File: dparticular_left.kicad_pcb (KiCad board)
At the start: 2 copper layers, 48 parts, among them J2 USB from outside, J3 To Right Hand, J4 Jumper to Teensy USB, SW1:6 Key_Scrl, SW1:7 Key_Paus, SW2:1 Key_ESC, SW2:2 Key_F1, SW2:3 Key_F2, SW2:4 Key_F3, SW2:5 Key_F4, SW2:6 Key_F5, SW2:7 Key_F6, SW3:1 Key_Home, SW3:2 Key_End, SW3:3 Key_Tilde, SW3:4 Key_1, SW3:5 Key_2, SW3:6 Key_3, SW3:7 Key_4, SW3:8 Key_5, SW4:2 Key_PgUp, SW4:3 Key_Tab, SW4:4 Key_Q, SW4:5 Key_W, SW4:6 Key_E, SW4:7 Key_R, SW4:8 Key_T, SW5:2 Key_PgDn, SW5:3 Key_Caps, SW5:4 Key_A, SW5:5 Key_S, SW5:6 Key_D, SW5:7 Key_F, SW5:8 Key_G, SW6:3 Key_LShft, SW6:4 Key_Z, SW6:5 Key_X, SW6:6 Key_C, SW6:7 Key_V, SW6:8 Key_B, SW7:3 Key_LCtrl, SW7:4 Key_Fn, SW7:5 Key_LWin, SW7:6 Key_LAlt, SW7:8 Key_LSpc, U2 TEENSY2.0_ONLY_EDGES

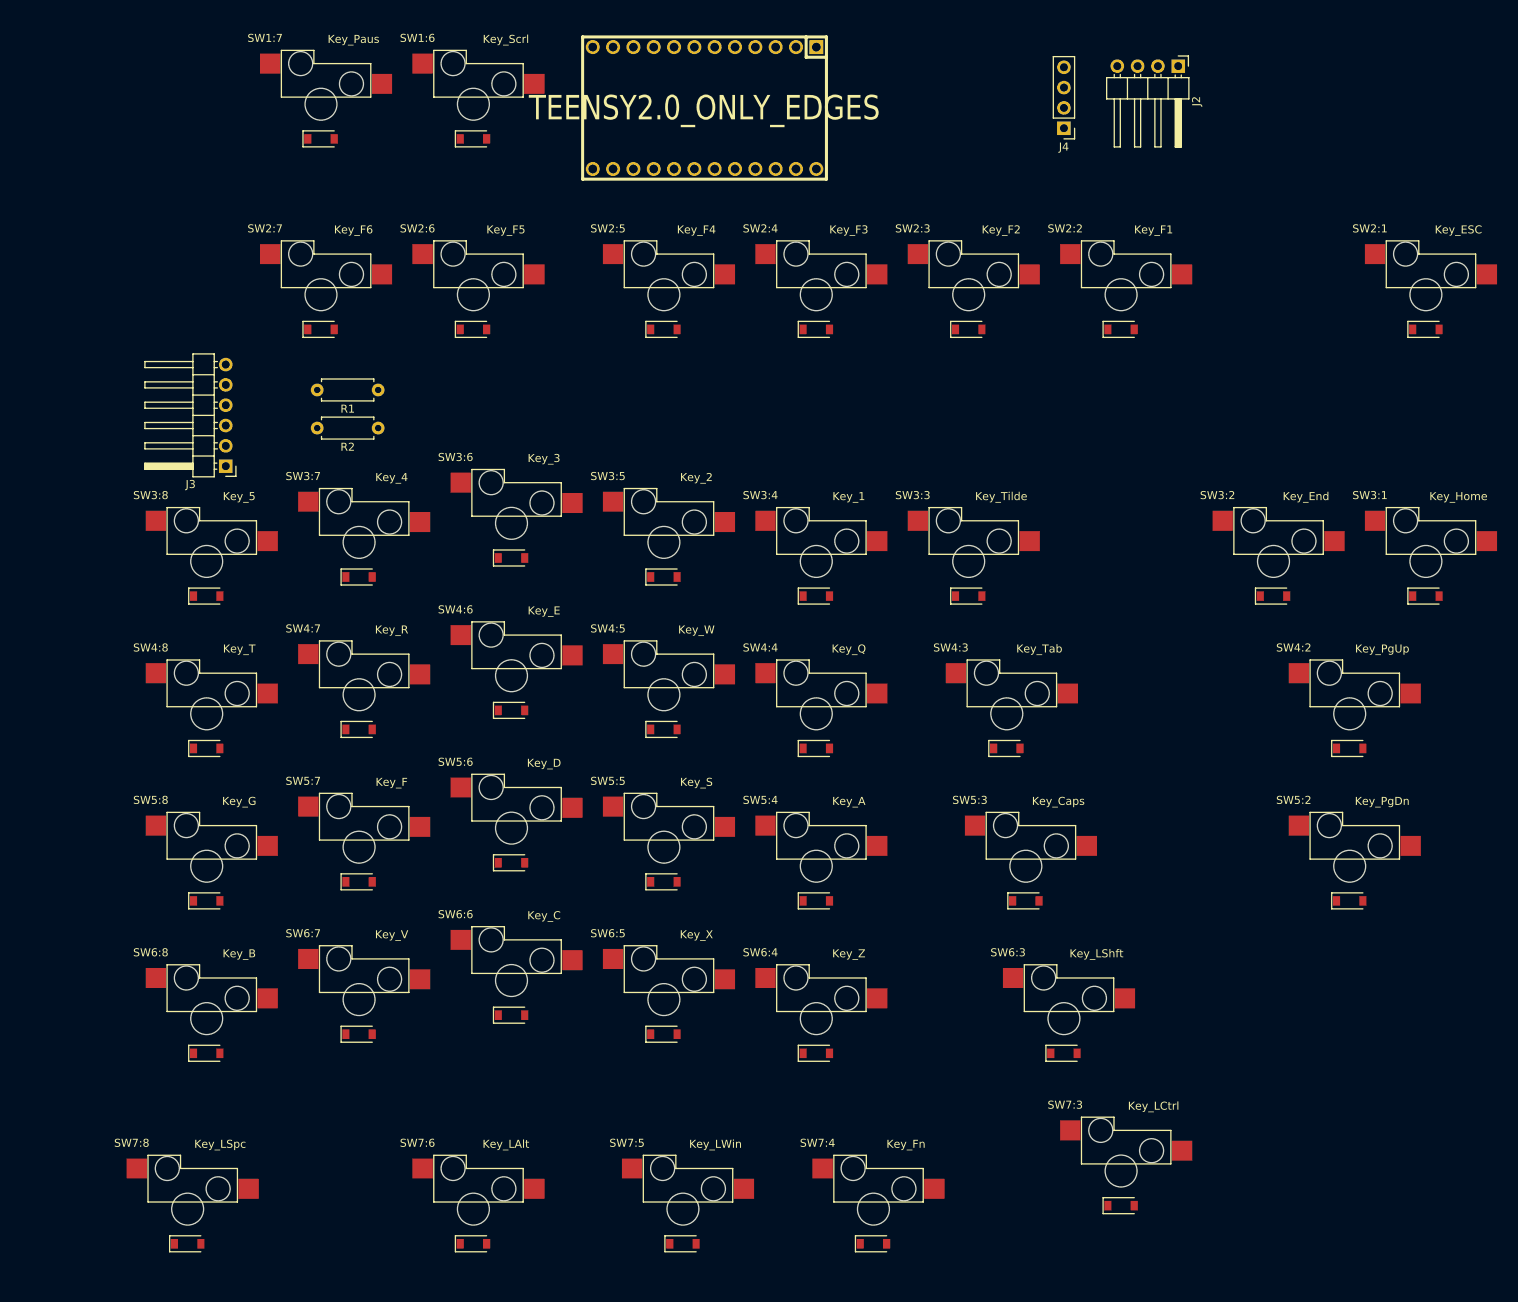
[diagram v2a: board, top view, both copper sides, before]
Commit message: Edge cuts, net list exports
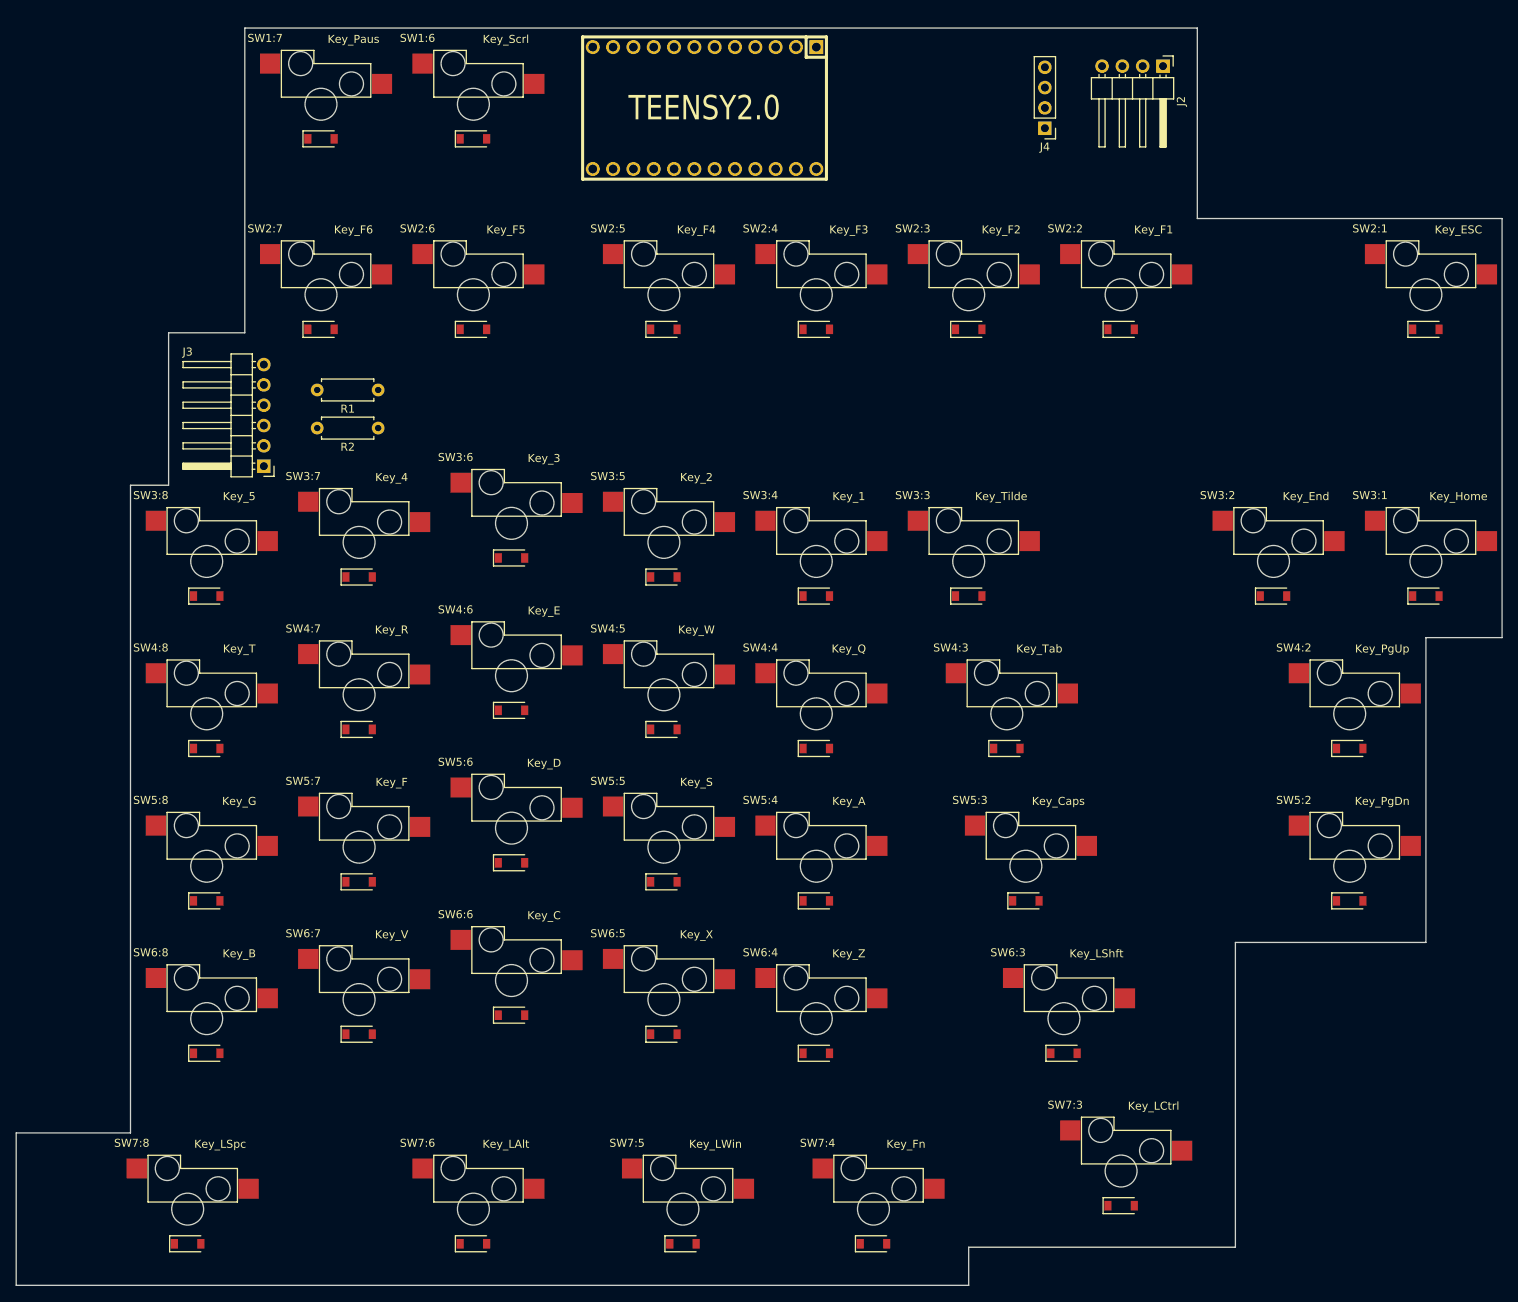
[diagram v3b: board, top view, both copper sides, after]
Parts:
- U2: value TEENSY2.0_ONLY_EDGES -> TEENSY2.0
- moved J3 4.76 mm to (50.0, 78.6)
- moved J4 2.38 mm to (147.6, 36.3)
- moved J2 1.91 mm to (162.4, 28.6)
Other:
- board outline added: 185.7 x 157.2 mm
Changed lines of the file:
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@@
   (general
     (thickness 1.6)
-    (drawings 33)
+    (drawings 51)
     (tracks 0)
     (zones 0)
@@
   )
   (module Connector_PinHeader_2.54mm:PinHeader_1x04_P2.54mm_Vertical (layer F.Cu)
-    (at 150.01875 36.3375 180)
+    (at 147.6375 36.3375 180)
     (descr "Through hole straight pin header, 1x04, 2.54mm pitch, single row")
     (tags "Through hole pin header THT 1x04 2.54mm single row")
@@
     )
     (fp_text value "Jumper to Teensy USB" (at 0 9.95) (layer F.Fab)
-      (effects (font (size 1 1) (thickness 0.15)))
-    )
-    (fp_text user %R (at 0 3.81 90) (layer F.Fab)
       (effects (font (size 1 1) (thickness 0.15)))
     )
@@
     (fp_line (start 1.8 9.4) (end 1.8 -1.8) (layer F.CrtYd) (width 0.05))
     (fp_line (start 1.8 -1.8) (end -1.8 -1.8) (layer F.CrtYd) (width 0.05))
+    (fp_text user %R (at 0 3.81 90) (layer F.Fab)
+      (effects (font (size 1 1) (thickness 0.15)))
+    )
     (pad 4 thru_hole oval (at 0 7.62 180) (size 1.7 1.7) (drill 1) (layers *.Cu *.Mask)
       (net 4 GND))
@@
   )
   (module Connector_PinHeader_2.54mm:PinHeader_1x06_P2.54mm_Horizontal (layer F.Cu)
-    (at 45.24375 78.58125 180)
+    (at 50.00625 78.58125 180)
     (descr "Through hole angled pin header, 1x06, 2.54mm pitch, 6mm pin length, single row")
     (tags "Through hole angled pin header THT 1x06 2.54mm single row")
-    (fp_text reference J3 (at 4.385 -2.27) (layer F.SilkS)
+    (fp_text reference J3 (at 9.525 14.2875) (layer F.SilkS)
       (effects (font (size 1 1) (thickness 0.15)))
     )
     (fp_text value "To Right Hand" (at 4.385 14.97) (layer F.Fab)
-      (effects (font (size 1 1) (thickness 0.15)))
-    )
-    (fp_text user %R (at 2.77 6.35 90) (layer F.Fab)
       (effects (font (size 1 1) (thickness 0.15)))
     )
@@
     (fp_line (start 10.55 14.5) (end 10.55 -1.8) (layer F.CrtYd) (width 0.05))
     (fp_line (start 10.55 -1.8) (end -1.8 -1.8) (layer F.CrtYd) (width 0.05))
+    (fp_text user %R (at 2.77 6.35 90) (layer F.Fab)
+      (effects (font (size 1 1) (thickness 0.15)))
+    )
     (pad 6 thru_hole oval (at 0 12.7 180) (size 1.7 1.7) (drill 1) (layers *.Cu *.Mask)
       (net 4 GND))
@@
   )
   (module Connector_PinHeader_2.54mm:PinHeader_1x04_P2.54mm_Horizontal (layer F.Cu)
-    (at 164.30625 28.575 270)
+    (at 162.40125 28.575 270)
     (descr "Through hole angled pin header, 1x04, 2.54mm pitch, 6mm pin length, single row")
     (tags "Through hole angled pin header THT 1x04 2.54mm single row")
@@
     )
     (fp_text value "USB from outside" (at 4.385 9.89 90) (layer F.Fab)
-      (effects (font (size 1 1) (thickness 0.15)))
-    )
-    (fp_text user %R (at 2.77 3.81) (layer F.Fab)
       (effects (font (size 1 1) (thickness 0.15)))
     )
@@
     (fp_line (start 10.55 9.4) (end 10.55 -1.8) (layer F.CrtYd) (width 0.05))
     (fp_line (start 10.55 -1.8) (end -1.8 -1.8) (layer F.CrtYd) (width 0.05))
+    (fp_text user %R (at 2.77 3.81) (layer F.Fab)
+      (effects (font (size 1 1) (thickness 0.15)))
+    )
     (pad 4 thru_hole oval (at 0 7.62 270) (size 1.7 1.7) (drill 1) (layers *.Cu *.Mask)
       (net 4 GND))
@@
       (effects (font (size 3.048 2.54) (thickness 0.4572)))
     )
-    (fp_text value TEENSY2.0_ONLY_EDGES (at 0 0) (layer F.SilkS)
+    (fp_text value TEENSY2.0 (at 0 0) (layer F.SilkS)
       (effects (font (size 3.048 2.54) (thickness 0.4572)))
     )
@@
       (net 4 GND))
   )
+  (gr_line (start 166.6875 23.8125) (end 47.625 23.8125) (layer Edge.Cuts) (width 0.05))
+  (gr_line (start 166.6875 47.625) (end 166.6875 23.8125) (layer Edge.Cuts) (width 0.05))
+  (gr_line (start 204.7875 47.625) (end 166.6875 47.625) (layer Edge.Cuts) (width 0.05))
+  (gr_line (start 204.7875 100.0125) (end 204.7875 47.625) (layer Edge.Cuts) (width 0.05))
+  (gr_line (start 195.2625 100.0125) (end 204.7875 100.0125) (layer Edge.Cuts) (width 0.05))
+  (gr_line (start 195.2625 138.1125) (end 195.2625 100.0125) (layer Edge.Cuts) (width 0.05))
+  (gr_line (start 171.45 138.1125) (end 195.2625 138.1125) (layer Edge.Cuts) (width 0.05))
+  (gr_line (start 171.45 176.2125) (end 171.45 138.1125) (layer Edge.Cuts) (width 0.05))
+  (gr_line (start 138.1125 176.2125) (end 171.45 176.2125) (layer Edge.Cuts) (width 0.05))
+  (gr_line (start 138.1125 180.975) (end 138.1125 176.2125) (layer Edge.Cuts) (width 0.05))
+  (gr_line (start 19.05 180.975) (end 138.1125 180.975) (layer Edge.Cuts) (width 0.05))
+  (gr_line (start 19.05 161.925) (end 19.05 180.975) (layer Edge.Cuts) (width 0.05))
+  (gr_line (start 33.3375 161.925) (end 19.05 161.925) (layer Edge.Cuts) (width 0.05))
+  (gr_line (start 33.3375 80.9625) (end 33.3375 161.925) (layer Edge.Cuts) (width 0.05))
+  (gr_line (start 38.1 80.9625) (end 33.3375 80.9625) (layer Edge.Cuts) (width 0.05))
+  (gr_line (start 38.1 61.9125) (end 38.1 80.9625) (layer Edge.Cuts) (width 0.05))
+  (gr_line (start 47.625 61.9125) (end 38.1 61.9125) (layer Edge.Cuts) (width 0.05))
+  (gr_line (start 47.625 23.8125) (end 47.625 61.9125) (layer Edge.Cuts) (width 0.05))
   (gr_line (start 142.875 157.1625) (end 171.45 157.1625) (layer F.Fab) (width 0.15))
   (gr_line (start 142.875 176.2125) (end 142.875 157.1625) (layer F.Fab) (width 0.15))

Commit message: Design rules compatible with common prototype board manufacturers
Maximums that work with JLCPCB, ALLPCB, and Elecrow
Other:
- net class Default: clearance 0.2 -> 0.254; trace_width 0.25 -> 0.254; via_dia 0.8 -> 0.635; via_drill 0.4 -> 0.381
- rule trace_clearance: 0.2 -> 0.254
- rule trace_min: 0.2 -> 0.2032
- rule via_min_drill: 0.3 -> 0.254
- rule via_min_size: 0.4 -> 0.5588

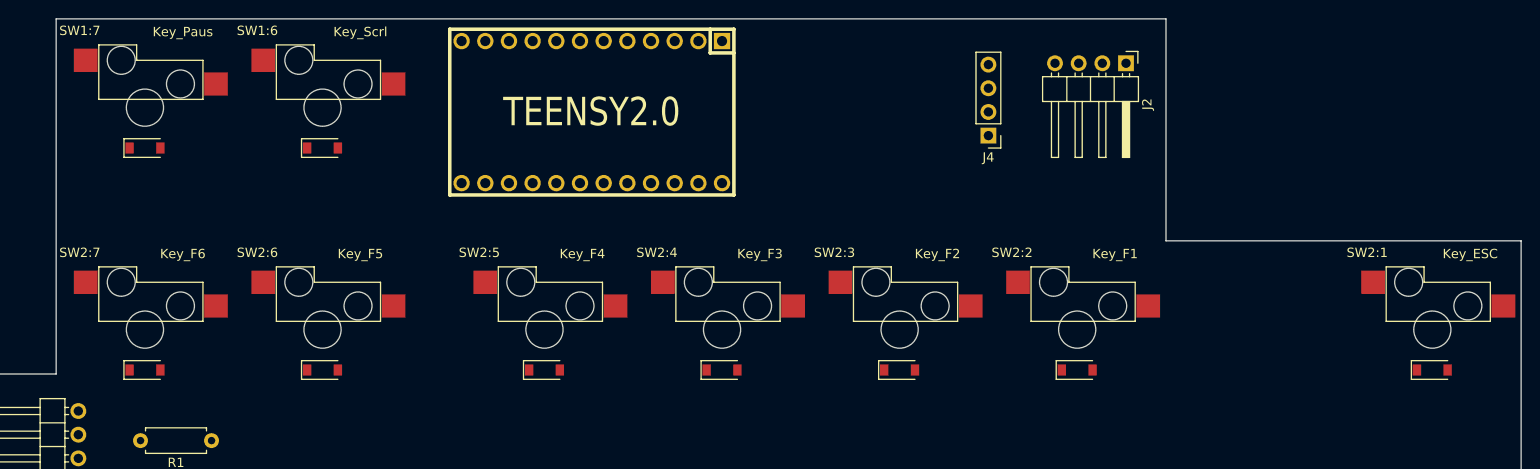
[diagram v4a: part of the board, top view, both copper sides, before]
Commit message: Moved USB headers to reduce width of top rectangle
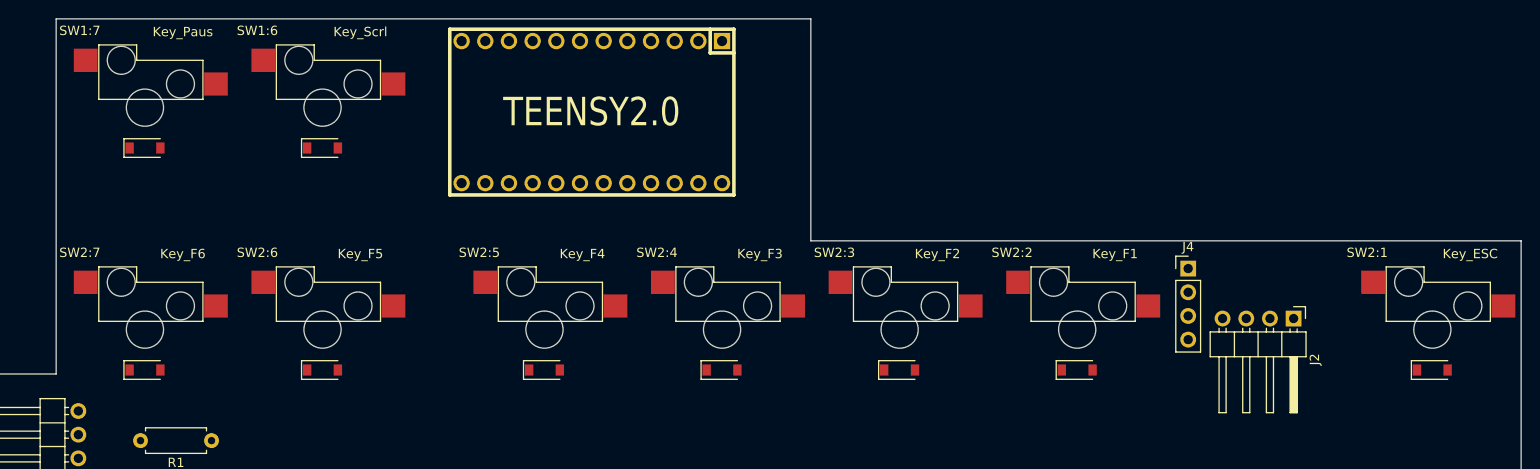
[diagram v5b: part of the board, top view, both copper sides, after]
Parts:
- moved J2 32.8 mm to (180.4, 56.0)
- moved J4 25.7 mm to (169.1, 50.6), turned to 0 degrees
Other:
- outline, holes or cut-outs redrawn
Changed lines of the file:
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@@
   )
   (module Connector_PinHeader_2.54mm:PinHeader_1x04_P2.54mm_Vertical (layer F.Cu)
-    (at 147.6375 36.3375 180)
+    (at 169.06864 50.601552)
     (descr "Through hole straight pin header, 1x04, 2.54mm pitch, single row")
     (tags "Through hole pin header THT 1x04 2.54mm single row")
@@
       (effects (font (size 1 1) (thickness 0.15)))
     )
-    (pad 4 thru_hole oval (at 0 7.62 180) (size 1.7 1.7) (drill 1) (layers *.Cu *.Mask)
+    (pad 4 thru_hole oval (at 0 7.62) (size 1.7 1.7) (drill 1) (layers *.Cu *.Mask)
       (net 4 GND))
-    (pad 3 thru_hole oval (at 0 5.08 180) (size 1.7 1.7) (drill 1) (layers *.Cu *.Mask)
+    (pad 3 thru_hole oval (at 0 5.08) (size 1.7 1.7) (drill 1) (layers *.Cu *.Mask)
       (net 3 /USB_DP))
-    (pad 2 thru_hole oval (at 0 2.54 180) (size 1.7 1.7) (drill 1) (layers *.Cu *.Mask)
+    (pad 2 thru_hole oval (at 0 2.54) (size 1.7 1.7) (drill 1) (layers *.Cu *.Mask)
       (net 2 /USB_DN))
-    (pad 1 thru_hole rect (at 0 0 180) (size 1.7 1.7) (drill 1) (layers *.Cu *.Mask)
+    (pad 1 thru_hole rect (at 0 0) (size 1.7 1.7) (drill 1) (layers *.Cu *.Mask)
       (net 1 +5V))
     (model ${KISYS3DMOD}/Connector_PinHeader_2.54mm.3dshapes/PinHeader_1x04_P2.54mm_Vertical.wrl
@@
   )
   (module Connector_PinHeader_2.54mm:PinHeader_1x04_P2.54mm_Horizontal (layer F.Cu)
-    (at 162.40125 28.575 270)
+    (at 180.379568 55.95936 270)
     (descr "Through hole angled pin header, 1x04, 2.54mm pitch, 6mm pin length, single row")
     (tags "Through hole angled pin header THT 1x04 2.54mm single row")
@@
       (net 4 GND))
   )
-  (gr_line (start 166.6875 23.8125) (end 47.625 23.8125) (layer Edge.Cuts) (width 0.05))
-  (gr_line (start 166.6875 47.625) (end 166.6875 23.8125) (layer Edge.Cuts) (width 0.05))
-  (gr_line (start 204.7875 47.625) (end 166.6875 47.625) (layer Edge.Cuts) (width 0.05))
+  (gr_line (start 128.587424 23.812512) (end 47.624992 23.812512) (layer Edge.Cuts) (width 0.05))
+  (gr_line (start 128.587424 47.624992) (end 128.587424 23.812512) (layer Edge.Cuts) (width 0.05))
+  (gr_line (start 204.78736 47.624992) (end 128.587424 47.624992) (layer Edge.Cuts) (width 0.05))
   (gr_line (start 204.7875 100.0125) (end 204.7875 47.625) (layer Edge.Cuts) (width 0.05))
   (gr_line (start 195.2625 100.0125) (end 204.7875 100.0125) (layer Edge.Cuts) (width 0.05))
